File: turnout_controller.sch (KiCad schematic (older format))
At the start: 27 parts, among them J1 DCC Input, J2 Conn_01x04, J3 Servo Motor, J4 LED Connect, SW1 SW_Push, SW2 SW_Push, U1 AP65111A, U2 MKE04P24M48SF0

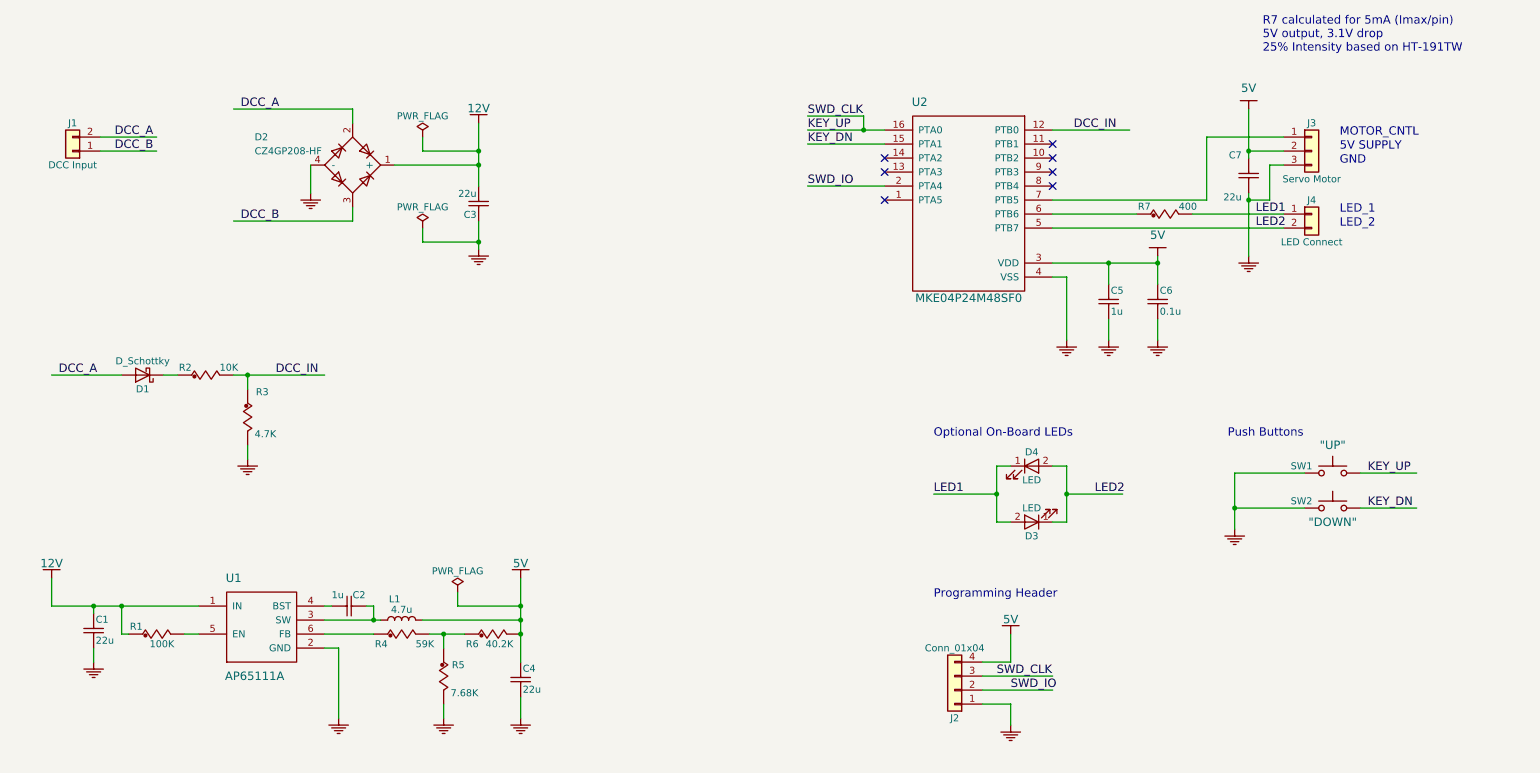
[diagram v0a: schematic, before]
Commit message: Connector improvements. Initial trace layout.
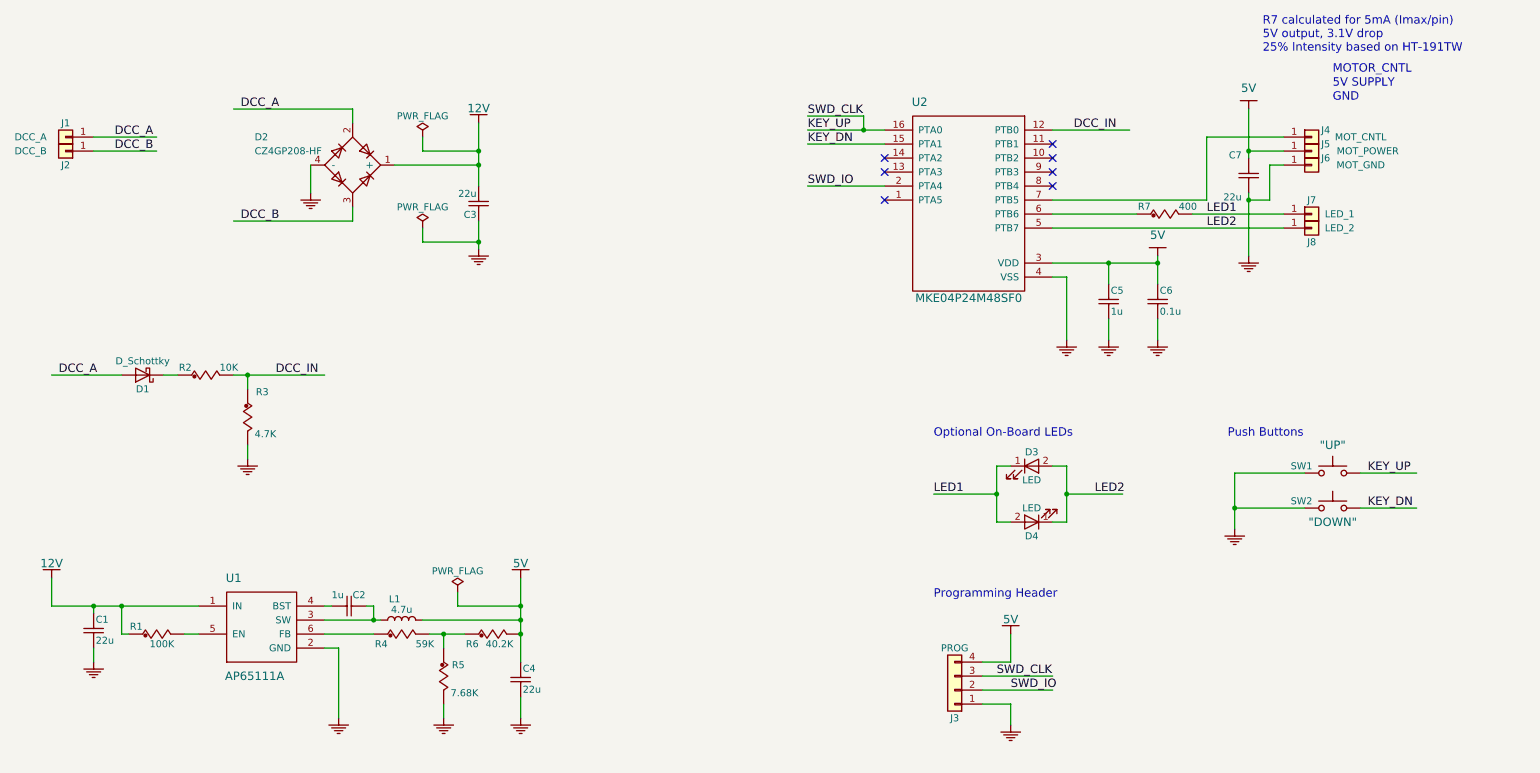
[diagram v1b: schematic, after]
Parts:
- removed J1: DCC Input, Socket_Strips:Socket_Strip_Straight_1x02_Pitch1.27mm, symbol Conn_01x02
- removed J3: Servo Motor, Socket_Strips:Socket_Strip_Straight_1x03_Pitch1.27mm, symbol Conn_01x03
- removed J4: LED Connect, Socket_Strips:Socket_Strip_Straight_1x02_Pitch1.27mm, symbol Conn_01x02
- added J1: DCC_A, half-connectors:Socket_Strip_Straight_1x01_Pitch1.27mm_at_edge, symbol Conn_01x01
- added J2: DCC_B, half-connectors:Socket_Strip_Straight_1x01_Pitch1.27mm_at_edge, symbol Conn_01x01
- added J4: MOT_CNTL, half-connectors:Socket_Strip_Straight_1x01_Pitch1.27mm_at_edge, symbol Conn_01x01
- added J5: MOT_POWER, half-connectors:Socket_Strip_Straight_1x01_Pitch1.27mm_at_edge, symbol Conn_01x01
- added J6: MOT_GND, half-connectors:Socket_Strip_Straight_1x01_Pitch1.27mm_at_edge, symbol Conn_01x01
- added J7: LED_1, half-connectors:Socket_Strip_Straight_1x01_Pitch1.27mm_at_edge, symbol Conn_01x01
- added J8: LED_2, half-connectors:Socket_Strip_Straight_1x01_Pitch1.27mm_at_edge, symbol Conn_01x01
- J3: renamed from J2; value Conn_01x04 -> PROG; footprint Socket_Strips:Socket_Strip_Straight_1x04_Pitch1.27mm -> half-connectors:Socket_Strip_Straight_1x04_Pitch1.27mm_at_edge
- renumbered D4 to D3, D3 to D4
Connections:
- wire segments 85 -> 86
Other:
- note removed: "LED_1"
- note removed: "LED_2"

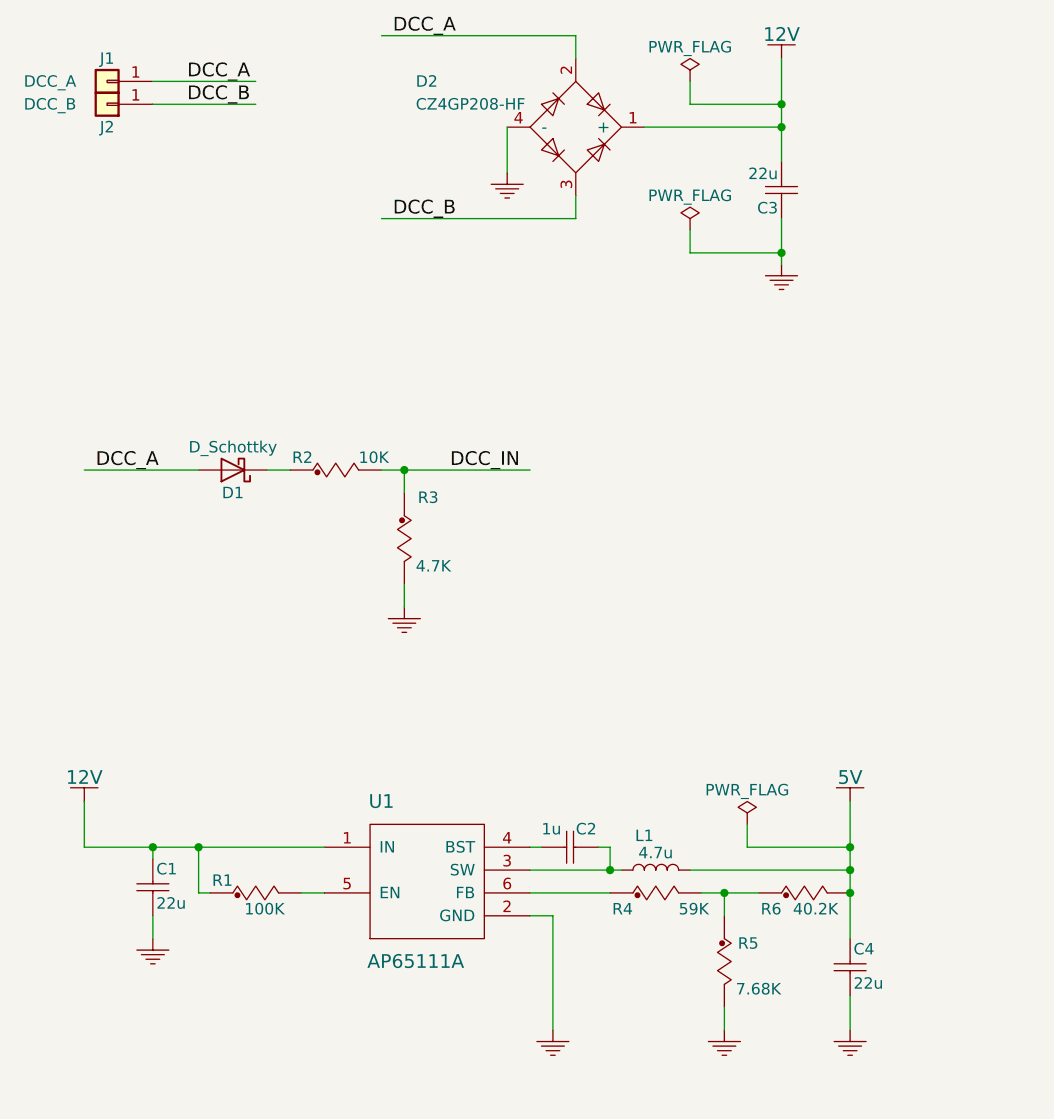
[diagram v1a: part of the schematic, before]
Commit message: Circuit updated with TPS561201 buck
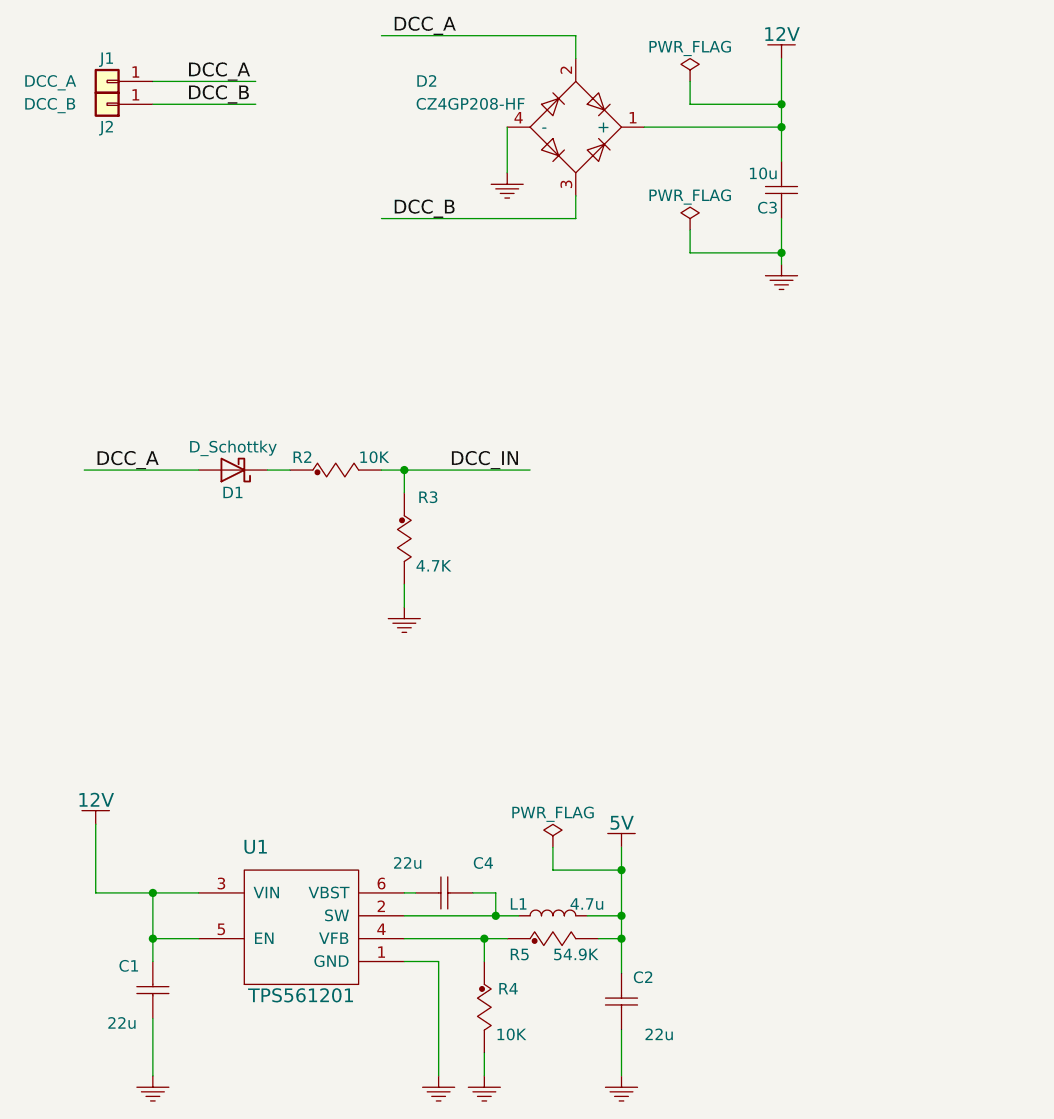
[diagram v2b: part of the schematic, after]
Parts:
- removed R1: 100K, Resistors_SMD:R_0603_HandSoldering, symbol RES
- removed R6: 40.2K, Resistors_SMD:R_0603_HandSoldering, symbol RES
- removed U1: AP65111A, TO_SOT_Packages_SMD:SOT-23-6, symbol AP65111A
- added U1: TPS561201, TO_SOT_Packages_SMD:SOT-23-6_Handsoldering, symbol TPS561201
- C2: value 1u -> 22u
- C3: value 22u -> 10u
- R4: value 59K -> 10K
- R5: value 7.68K -> 54.9K
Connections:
- wire segments 86 -> 83
